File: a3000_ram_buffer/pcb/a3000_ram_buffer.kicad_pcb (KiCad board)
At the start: 2 copper layers, 167 x 49.4 mm, 42 parts

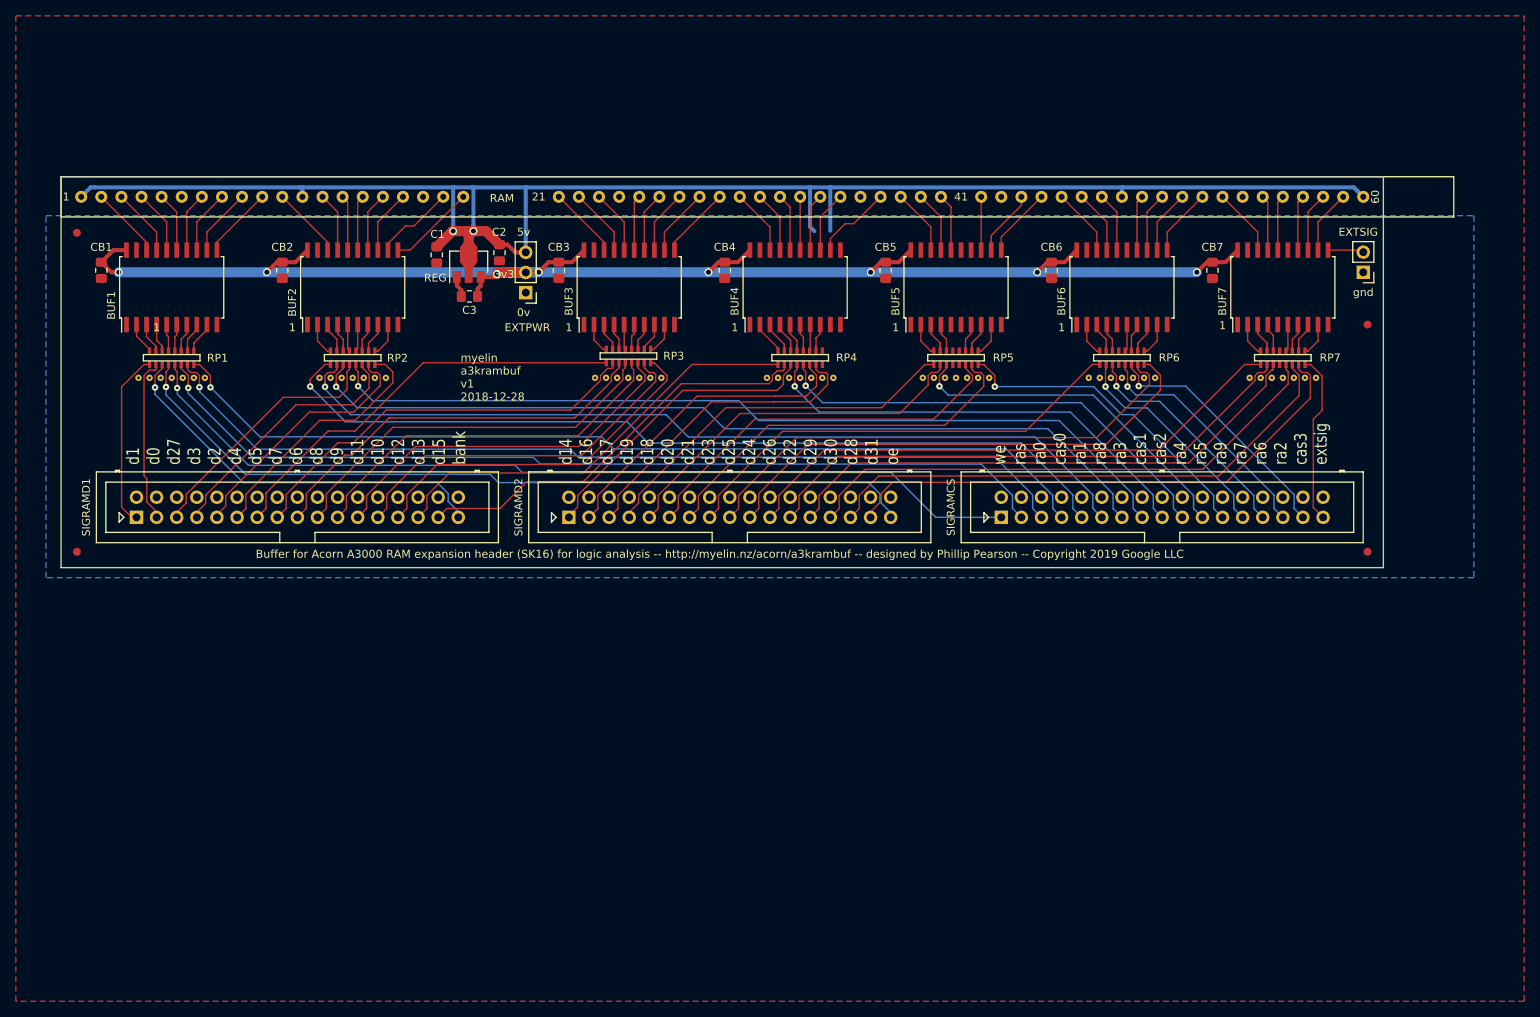
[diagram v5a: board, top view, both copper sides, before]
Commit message: Added a bunch of ground layer staples to keep everything together
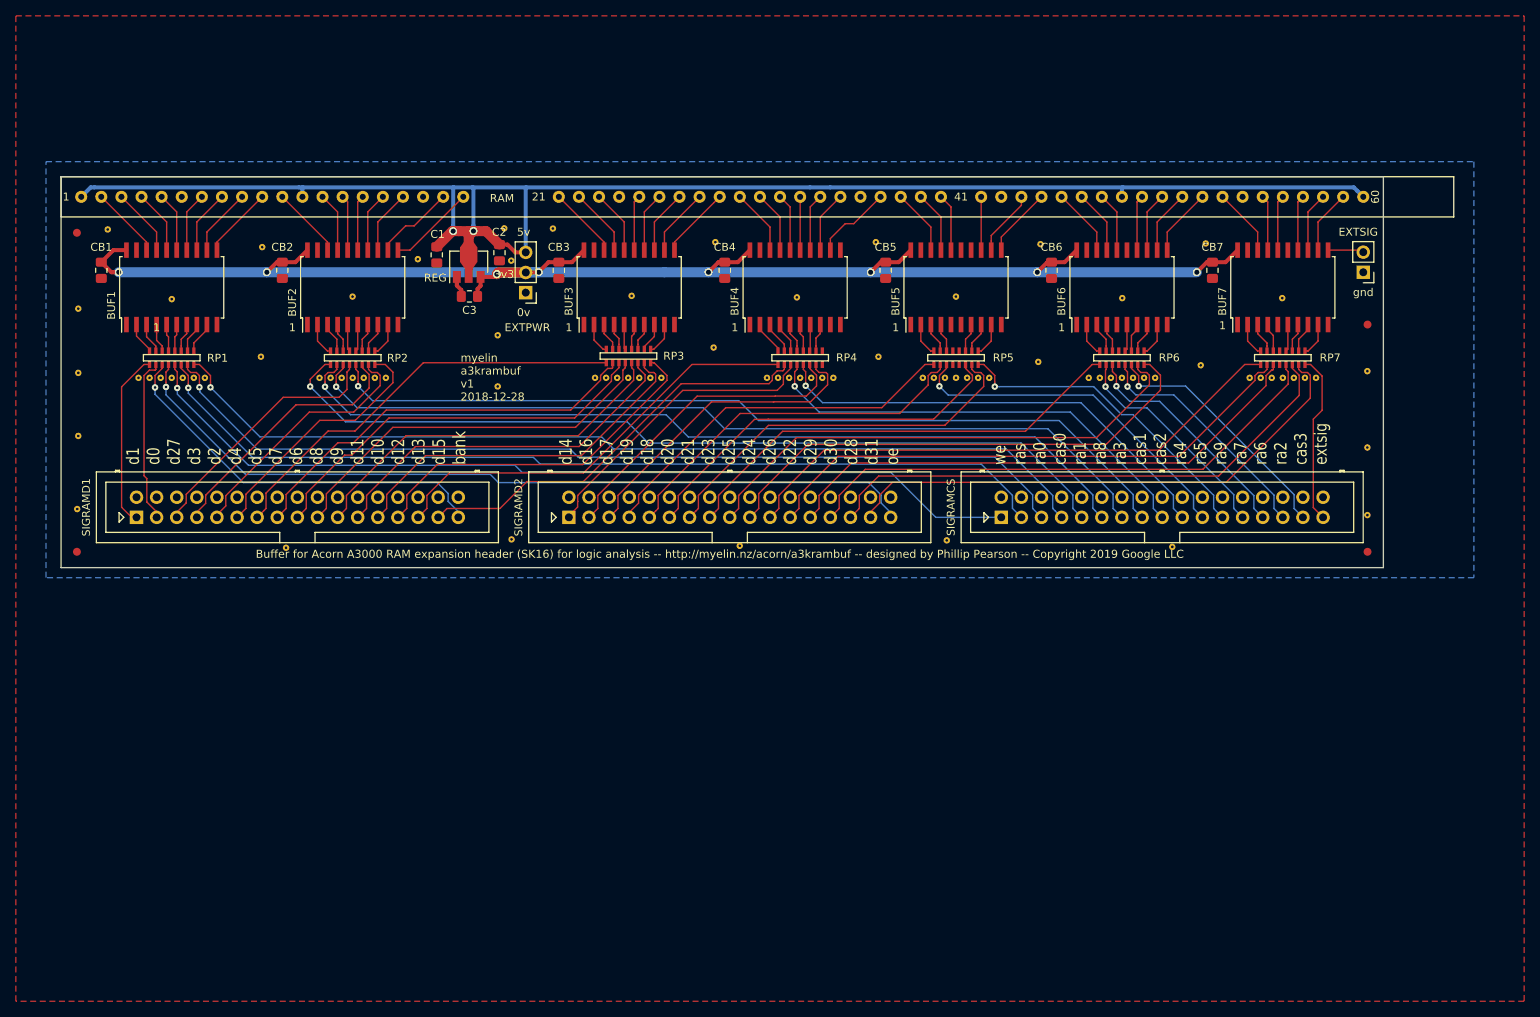
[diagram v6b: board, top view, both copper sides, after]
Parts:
- added staple_single1: , myelin-kicad:via_single, F.Cu at (61.6, 59.7)
- added staple_single10: , myelin-kicad:via_single, F.Cu at (129.1, 66.0)
- added staple_single11: , myelin-kicad:via_single, F.Cu at (139.1, 59.1)
- added staple_single12: , myelin-kicad:via_single, F.Cu at (42.1, 57.5)
- added staple_single13: , myelin-kicad:via_single, F.Cu at (91.3, 77.3)
- added staple_single14: , myelin-kicad:via_single, F.Cu at (91.3, 70.8)
- added staple_single15: , myelin-kicad:via_single, F.Cu at (149.2, 65.9)
- added staple_single16: , myelin-kicad:via_single, F.Cu at (61.4, 73.5)
- added staple_single17: , myelin-kicad:via_single, F.Cu at (118.6, 72.4)
- added staple_single18: , myelin-kicad:via_single, F.Cu at (139.4, 73.5)
- added staple_single19: , myelin-kicad:via_single, F.Cu at (159.6, 74.2)
- added staple_single2: , myelin-kicad:via_single, F.Cu at (190.4, 66.1)
- added staple_single20: , myelin-kicad:via_single, F.Cu at (180.1, 74.6)
- added staple_single21: , myelin-kicad:via_single, F.Cu at (92.2, 57.3)
- added staple_single22: , myelin-kicad:via_single, F.Cu at (81.3, 61.2)
- added staple_single23: , myelin-kicad:via_single, F.Cu at (93.1, 61.4)
- added staple_single24: , myelin-kicad:via_single, F.Cu at (98.3, 57.3)
- added staple_single25: , myelin-kicad:via_single, F.Cu at (201.2, 75.4)
- added staple_single26: , myelin-kicad:via_single, F.Cu at (38.4, 67.5)
- added staple_single27: , myelin-kicad:via_single, F.Cu at (38.2, 92.8)
- added staple_single28: , myelin-kicad:via_single, F.Cu at (93.1, 96.6)
- added staple_single29: , myelin-kicad:via_single, F.Cu at (64.6, 97.7)
- added staple_single3: , myelin-kicad:via_single, F.Cu at (73.0, 65.9)
- added staple_single30: , myelin-kicad:via_single, F.Cu at (148.1, 96.7)
- added staple_single31: , myelin-kicad:via_single, F.Cu at (38.4, 75.6)
- added staple_single32: , myelin-kicad:via_single, F.Cu at (201.2, 93.5)
- added staple_single33: , myelin-kicad:via_single, F.Cu at (201.2, 85.0)
- added staple_single34: , myelin-kicad:via_single, F.Cu at (121.9, 97.4)
- added staple_single35: , myelin-kicad:via_single, F.Cu at (176.5, 97.5)
- added staple_single36: , myelin-kicad:via_single, F.Cu at (38.4, 83.5)
- added staple_single4: , myelin-kicad:via_single, F.Cu at (180.8, 59.2)
- added staple_single5: , myelin-kicad:via_single, F.Cu at (118.8, 59.1)
- added staple_single6: , myelin-kicad:via_single, F.Cu at (108.3, 65.8)
- added staple_single7: , myelin-kicad:via_single, F.Cu at (159.9, 59.3)
- added staple_single8: , myelin-kicad:via_single, F.Cu at (50.2, 66.3)
- added staple_single9: , myelin-kicad:via_single, F.Cu at (170.2, 66.1)
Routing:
- net 5V: track 215.6 -> 204.4 mm
